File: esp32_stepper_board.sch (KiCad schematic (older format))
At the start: 36 parts, among them J1 Serial, J10 Conn_02x03_Odd_Even, J11 Micro_SD_Card, J2 Servo, J3 Stepper A/X, J4 Stepper B/Y, J5 Stepper C/Y, J6 Endstop A/X, J7 Endstop B/Y, J8 Endstop C/Z, J9 DC_PWR, SW1 SW_Push, SW2 SW_Push, SW3 Rotary_Encoder_Switch, U1 LM1117-5.0, U2 LM1117-3.3, U3 OLED_I2C, U5 STEPSTICK, U6 STEPSTICK, U7 STEPSTICK

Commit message: Updated pins, added I2C GPIO expander
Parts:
- removed J10: Conn_02x03_Odd_Even, symbol Conn_02x03_Odd_Even
- added C10, C3: 100n, symbol C
- added C11, C12, C13: 100u, symbol CP
- added C7: 1n, symbol C
- added D1: PWR_LED, symbol LED
- added R3: 100, symbol R
- added SW?: SW_Push, symbol SW_Push
- added U3: PCF8574, symbol PCF8574
- C6: renamed from C2; value 0.1u -> 100n
- C9: renamed from C7; value 0.1u -> 100n
- R2: value 10k -> 470
- gave numbers to parts that had none: 1
- renumbered C3 to C2, C6 to C8, J11 to J10, R3 to R4, R4 to R5, R5 to R6, R6 to R7, R7 to R8, R8 to R9, U3 to U4, U5 to U6, U6 to U7, U7 to U8
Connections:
- net labels added: SCL1, SDA1, ~ES_A/X, ~ES_B/Y, ~ES_C/Z, ~PAUSE, ~PCFA_INT
- net labels removed: DIS_SCL, DIS_SDA, ES_A/X, ES_B/Y, ES_C/Z, OLED_SCL, OLED_SDA
- wire segments 182 -> 210
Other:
- note added: "Check power up reset/run circuit from datasheet"
- note added: "I2C GPIO Expander (PCF8574)"
- moved on the sheet: C1, C2, C4, C5, C6, C8, C9, J1, J10, J2, J3, J4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

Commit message: Updated schematic & pdf
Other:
- note added: "Pause button?"
- note removed: "Check power up reset/run circuit from datasheet"
- moved on the sheet: C10, C3, C6, C7, C8, C9, D1, J10, R1, R2, R3, R4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

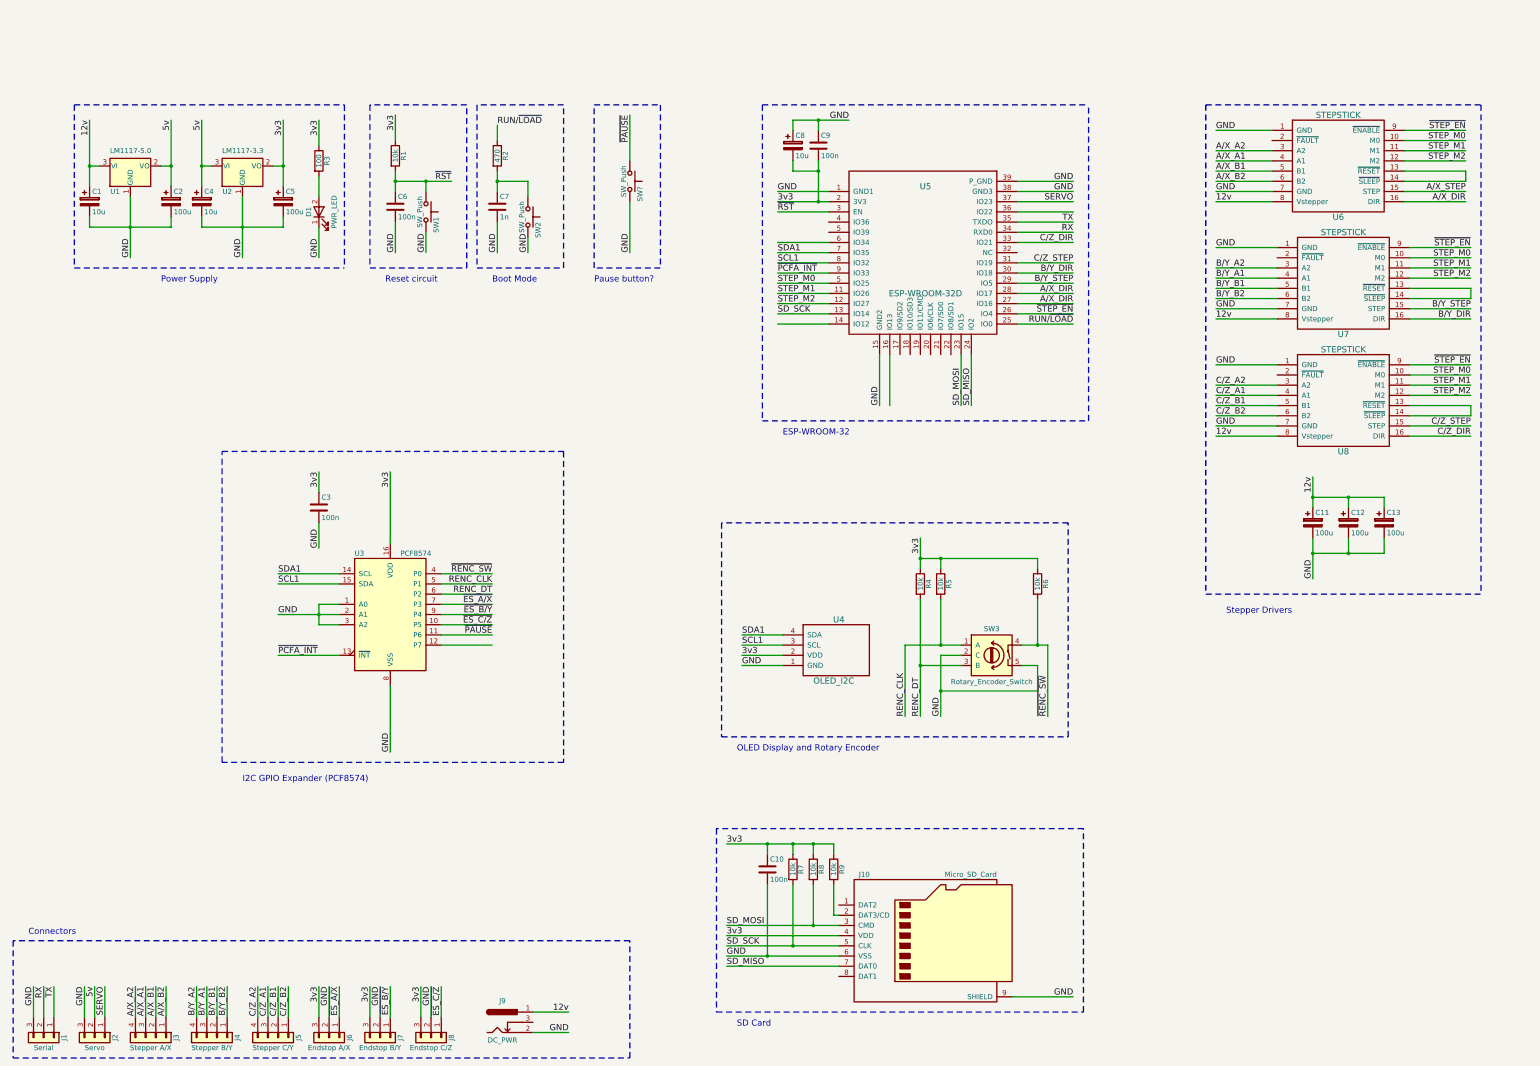
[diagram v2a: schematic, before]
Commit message: Pin optimzation and aux ports
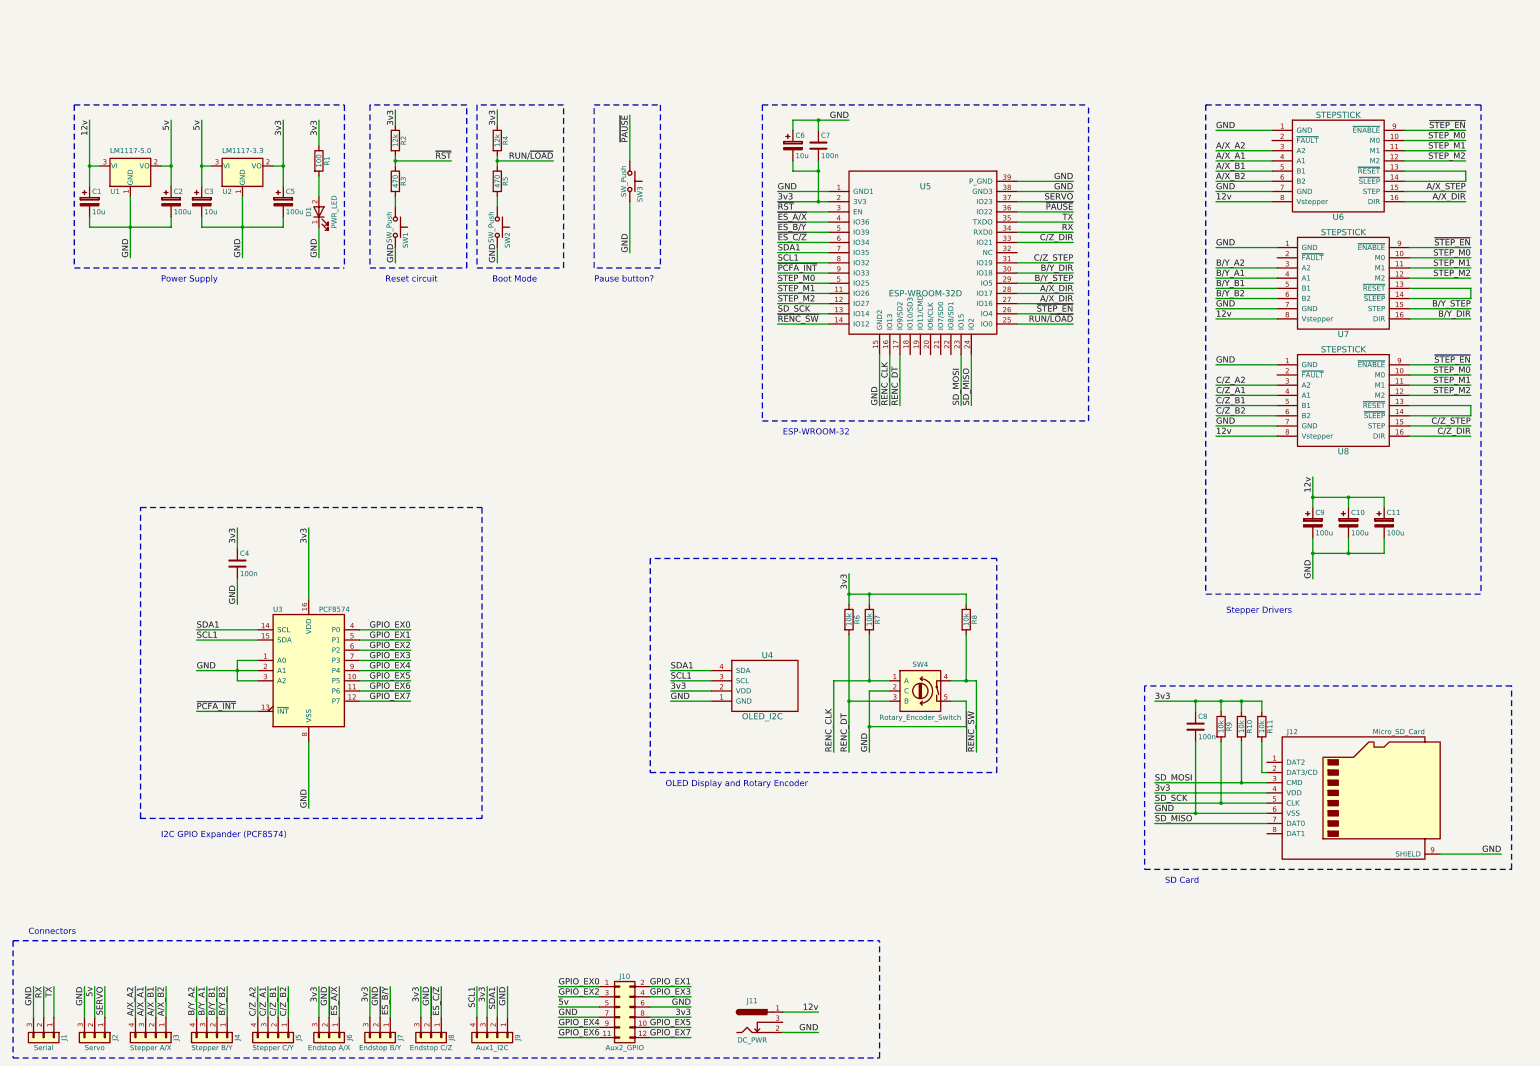
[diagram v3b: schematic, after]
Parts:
- removed C6: 100n, symbol C
- removed C7: 1n, symbol C
- added J10: Aux2_GPIO, symbol Conn_02x06_Odd_Even
- added J9: Aux1_I2C, symbol Conn_01x04
- added R3, R5: 470, symbol R
- R2: renamed from R1; value 10k -> 12k
- R4: renamed from R2; value 470 -> 12k
- gave numbers to parts that had none: 1
- renumbered C12 to C10, C13 to C11, C4 to C3, C3 to C4, C8 to C6, C9 to C7, C10 to C8, C11 to C9, J9 to J11, J10 to J12, R3 to R1, R8 to R10, R9 to R11, R4 to R6, R5 to R7, R6 to R8, R7 to R9, SW3 to SW4
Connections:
- net 3v3: now also R4.1, J10.8 (Pin_8), J9.3 (Pin_3)
- net 5v: now also J10.5 (Pin_5)
- net GND: now also J10.6 (Pin_6), J10.7 (Pin_7), J9.1 (Pin_1)
- net RENC_CLK: now also U5.16 (IO13); no longer U3.5 (P1)
- net RENC_DT: now also U5.17 (IO9/SD2); no longer U3.6 (P2)
- net RUN/~LOAD: now also R4.2, R5.1; no longer R4.1
- net SCL1: now also J9.4 (Pin_4)
- net SDA1: now also J9.2 (Pin_2)
- net ~ES_A/X: now also U5.4 (IO36); no longer U3.7 (P3)
- net ~ES_B/Y: now also U5.5 (IO39); no longer U3.9 (P4)
- net ~ES_C/Z: now also U5.6 (IO34); no longer U3.10 (P5)
- net ~PAUSE: now also U5.36 (IO22); no longer U3.11 (P6)
- net ~RENC_SW: now also U5.14 (IO12); no longer U3.4 (P0)
- net ~RST: now also R3.1; no longer SW1.1
- net at SW2.1: now also R5.2; no longer R4.2
- net GPIO_EX7: now reaches U3.12 (P7)
- net GPIO_EX7: now also J10.12 (Pin_12)
- new net: R3.2, SW1.1
- new net GPIO_EX0: J10.1 (Pin_1), U3.4 (P0)
- new net GPIO_EX1: J10.2 (Pin_2), U3.5 (P1)
- new net GPIO_EX2: J10.3 (Pin_3), U3.6 (P2)
- new net GPIO_EX3: J10.4 (Pin_4), U3.7 (P3)
- new net GPIO_EX4: J10.9 (Pin_9), U3.9 (P4)
- new net GPIO_EX5: J10.10 (Pin_10), U3.10 (P5)
- new net GPIO_EX6: J10.11 (Pin_11), U3.11 (P6)
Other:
- moved on the sheet: C4, C8, J11, J12, R10, R11, R2, R4, R6, R7, R8, R9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

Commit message: I2C Pull-ups
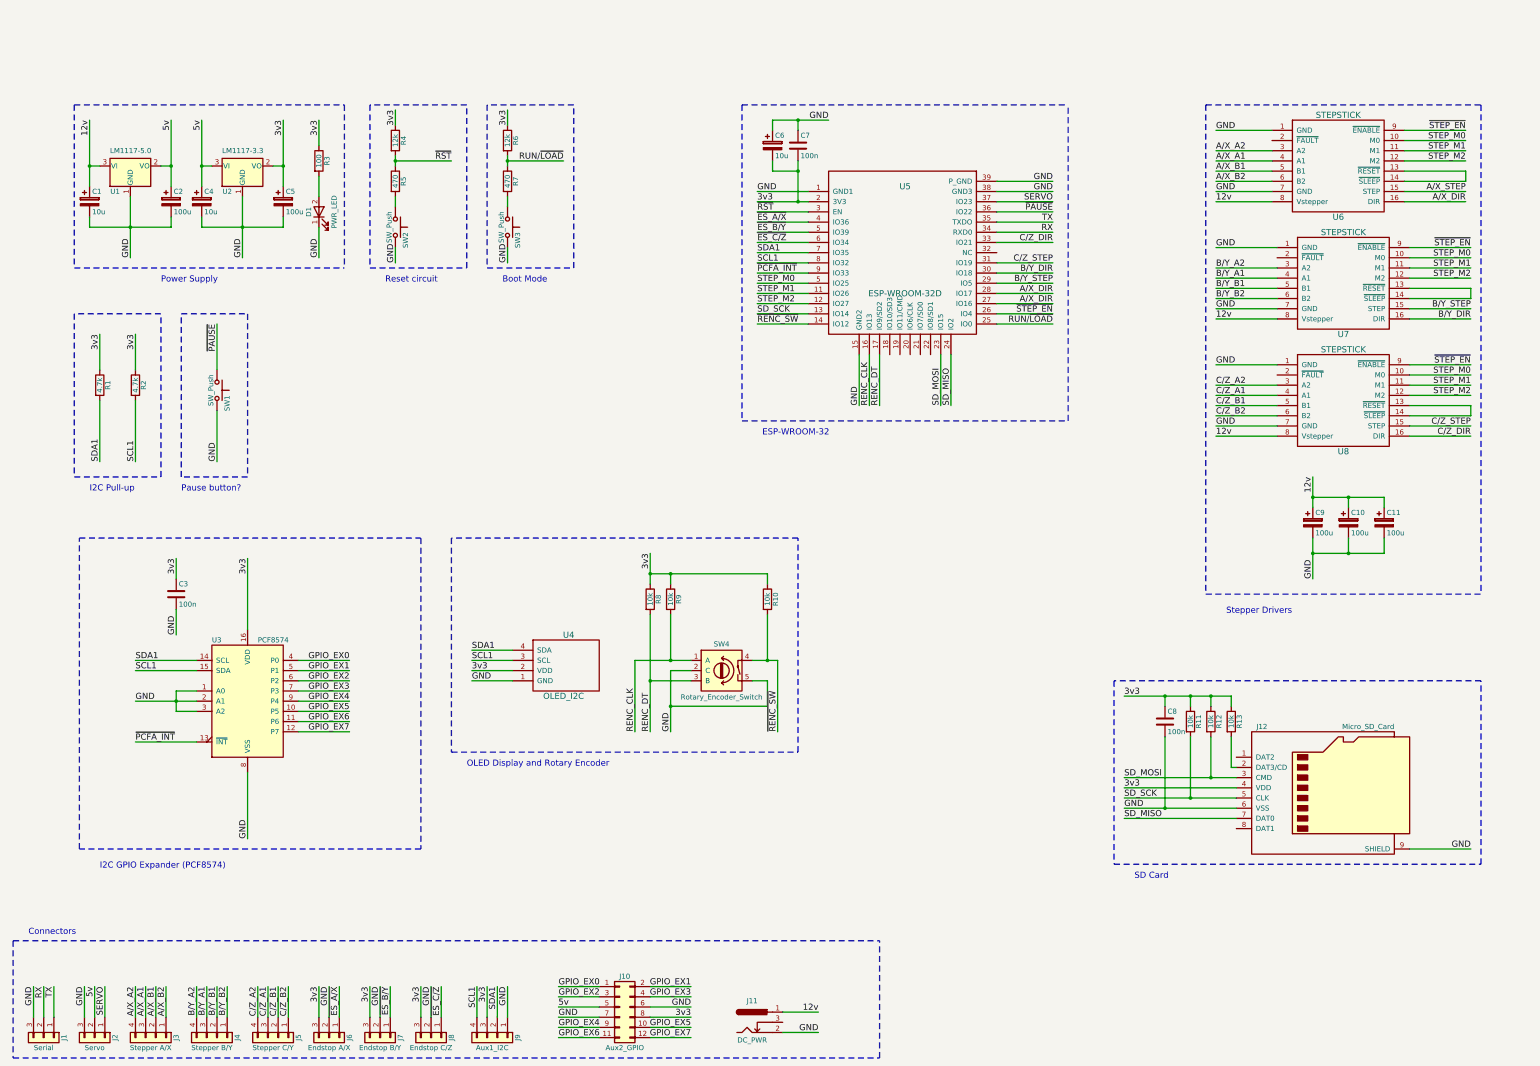
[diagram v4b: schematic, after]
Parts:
- added R1, R2: 4.7k, symbol R
- renumbered C4 to C3, C3 to C4, R8 to R10, R9 to R11, R10 to R12, R11 to R13, R1 to R3, R2 to R4, R3 to R5, R4 to R6, R5 to R7, R6 to R8, R7 to R9, SW3 to SW1, SW1 to SW2, SW2 to SW3
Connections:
- net 3v3: now also R1.1, R2.1
- net SCL1: now also R2.2
- net SDA1: now also R1.2
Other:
- note added: "I2C Pull-up"
- moved on the sheet: C3, C6, C7, C8, J12, R10, R11, R12, R13, R6, R7, R8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

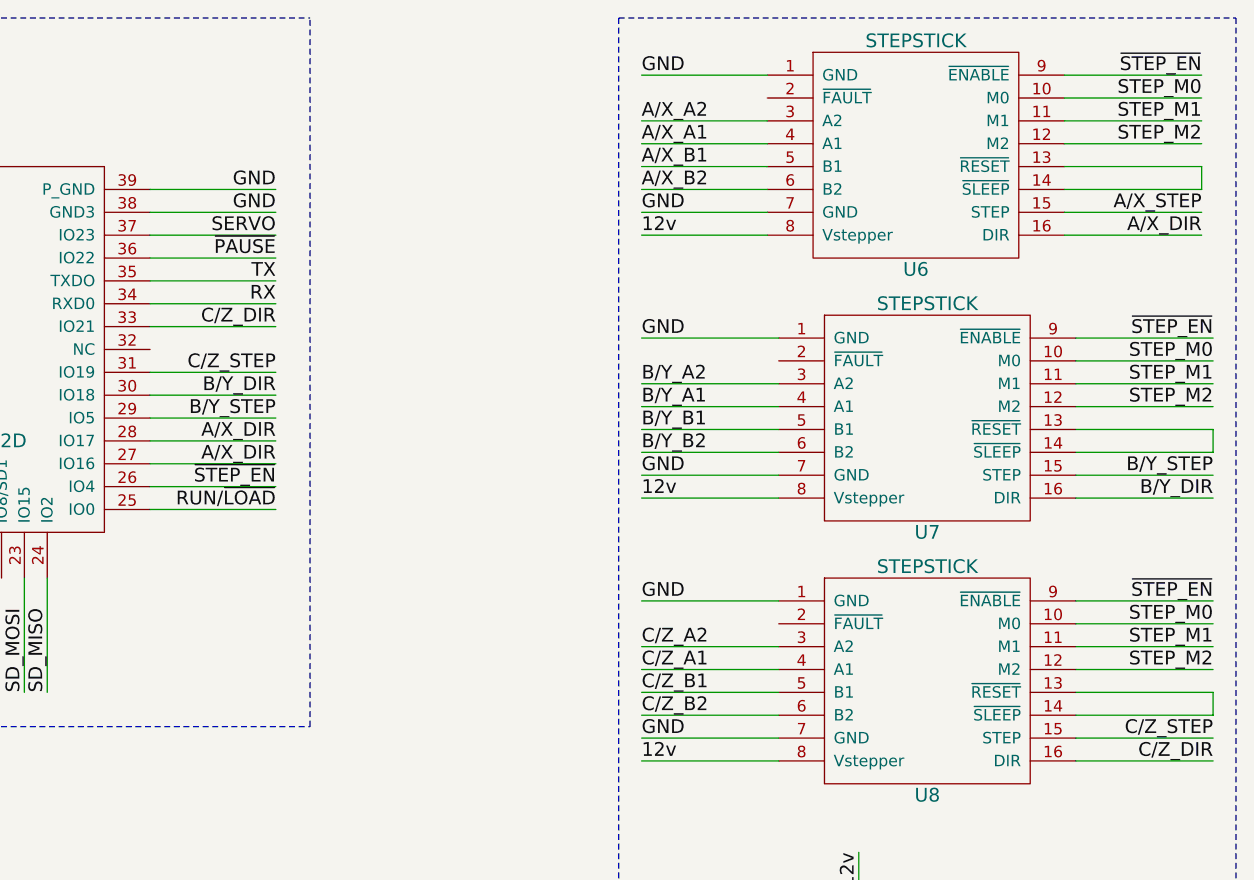
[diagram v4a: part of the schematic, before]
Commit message: Fix stepper reset & sleep
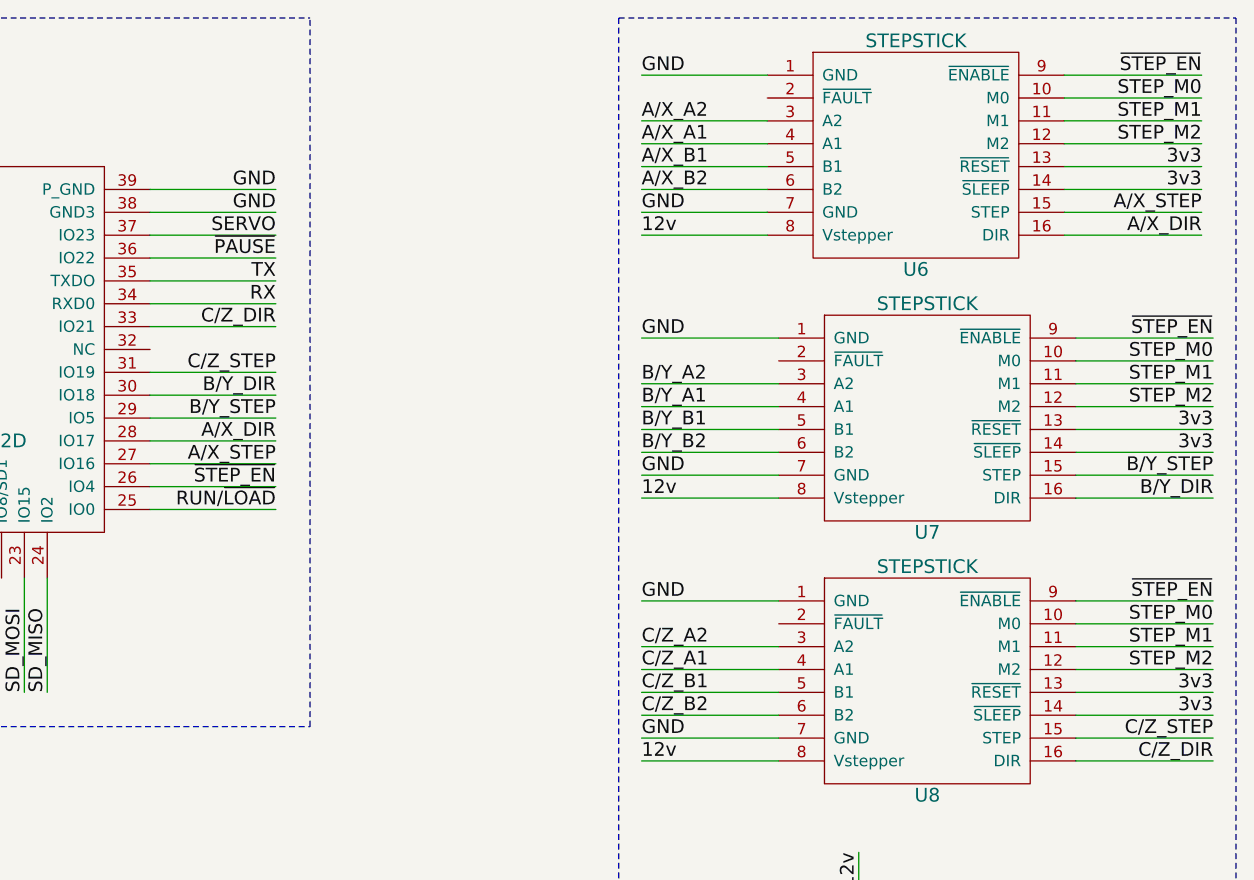
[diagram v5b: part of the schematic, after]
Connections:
- net 3v3: now also U6.13 (~RESET), U6.14 (~SLEEP), U7.13 (~RESET), U7.14 (~SLEEP), U8.13 (~RESET), U8.14 (~SLEEP)
- net A/X_DIR: no longer U5.27 (IO16)
- net A/X_STEP: now also U5.27 (IO16)
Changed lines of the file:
@@
 Text Label 10850 2750 2    60   ~ 0
 RX
-Text Label 10850 3450 2    60   ~ 0
-A/X_DIR
 Text Label 10850 3350 2    60   ~ 0
 A/X_DIR
@@
 	14300 1750 14900 1750
 Wire Wire Line
-	14900 2250 14900 2150
-Wire Wire Line
 	14350 3400 14950 3400
 Wire Wire Line
-	14950 3400 14950 3300
-Wire Wire Line
 	14950 3300 14350 3300
 Wire Wire Line
 	14350 4450 14950 4450
 Wire Wire Line
-	14950 4450 14950 4550
-Wire Wire Line
 	14950 4550 14350 4550
 Wire Wire Line
@@
 Wire Wire Line
 	10300 3250 10850 3250
-Wire Wire Line
-	10300 3150 10850 3150
 Wire Wire Line
 	10300 3050 10850 3050
@@
 Text Label 1850 5000 1    60   ~ 0
 SCL1
+Text Label 14900 2150 2    60   ~ 0
+3v3
+Text Label 14900 2250 2    60   ~ 0
+3v3
+Text Label 14950 3300 2    60   ~ 0
+3v3
+Text Label 14950 3400 2    60   ~ 0
+3v3
+Text Label 14950 4450 2    60   ~ 0
+3v3
+Text Label 14950 4550 2    60   ~ 0
+3v3
+Wire Wire Line
+	10300 3150 10850 3150
+Text Label 10850 3450 2    60   ~ 0
+A/X_STEP
 $EndSCHEMATC
